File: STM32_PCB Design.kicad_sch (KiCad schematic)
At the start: 17 parts, among them J1 USB_B_Micro, SW1 SW_SPDT, U1 STM32F103C8T6, Y1 16MHz

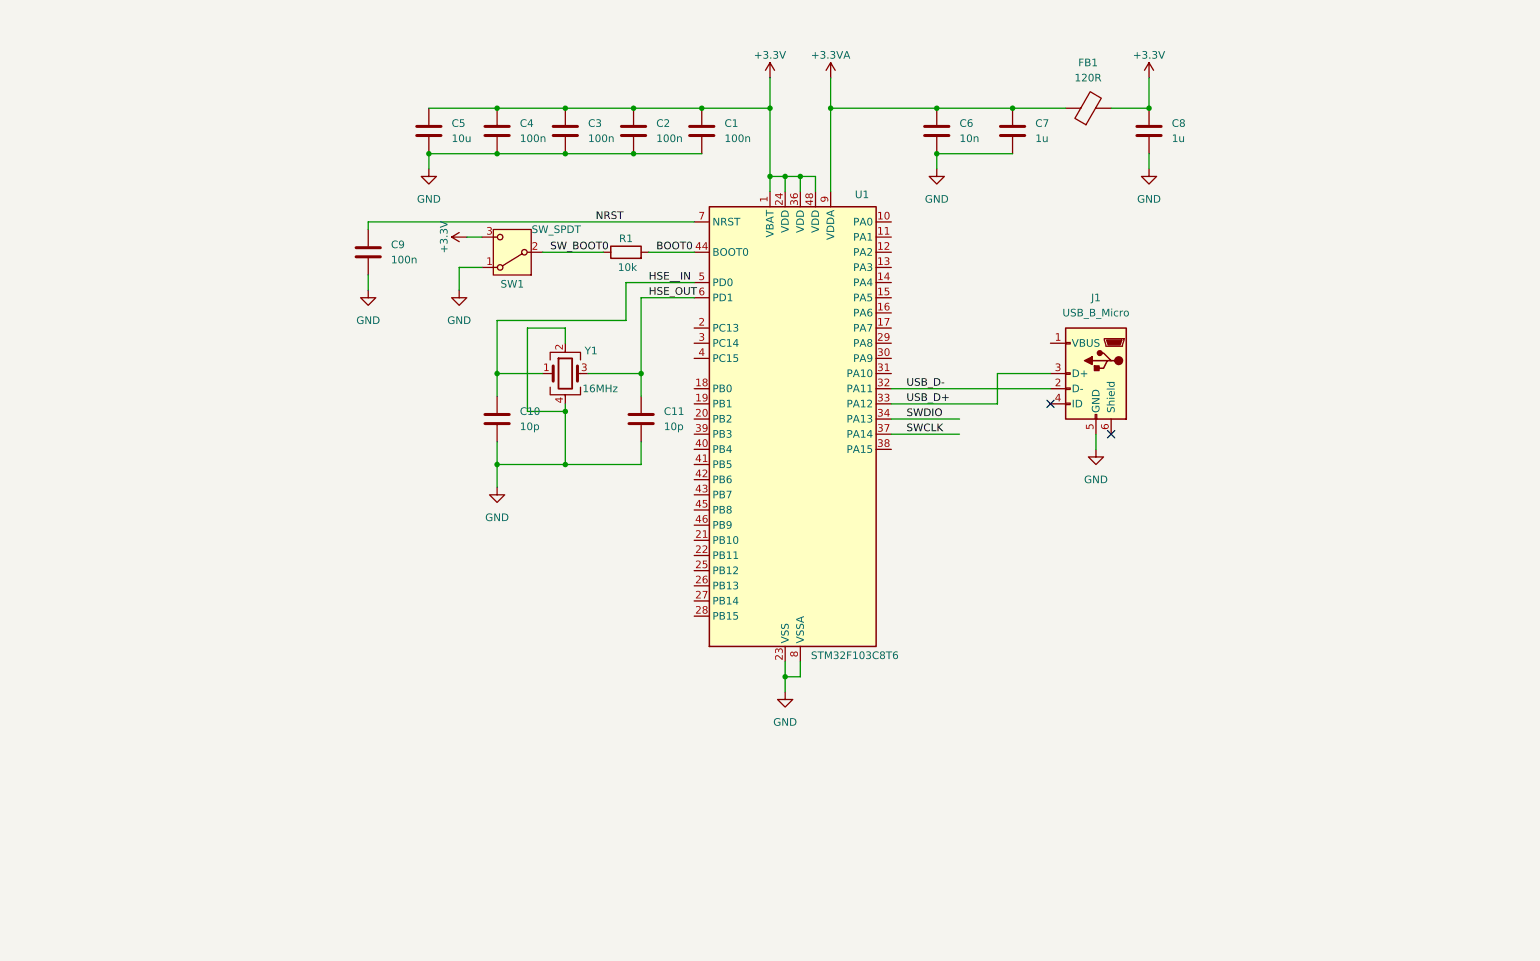
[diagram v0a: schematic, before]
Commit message: Added USART and I2C
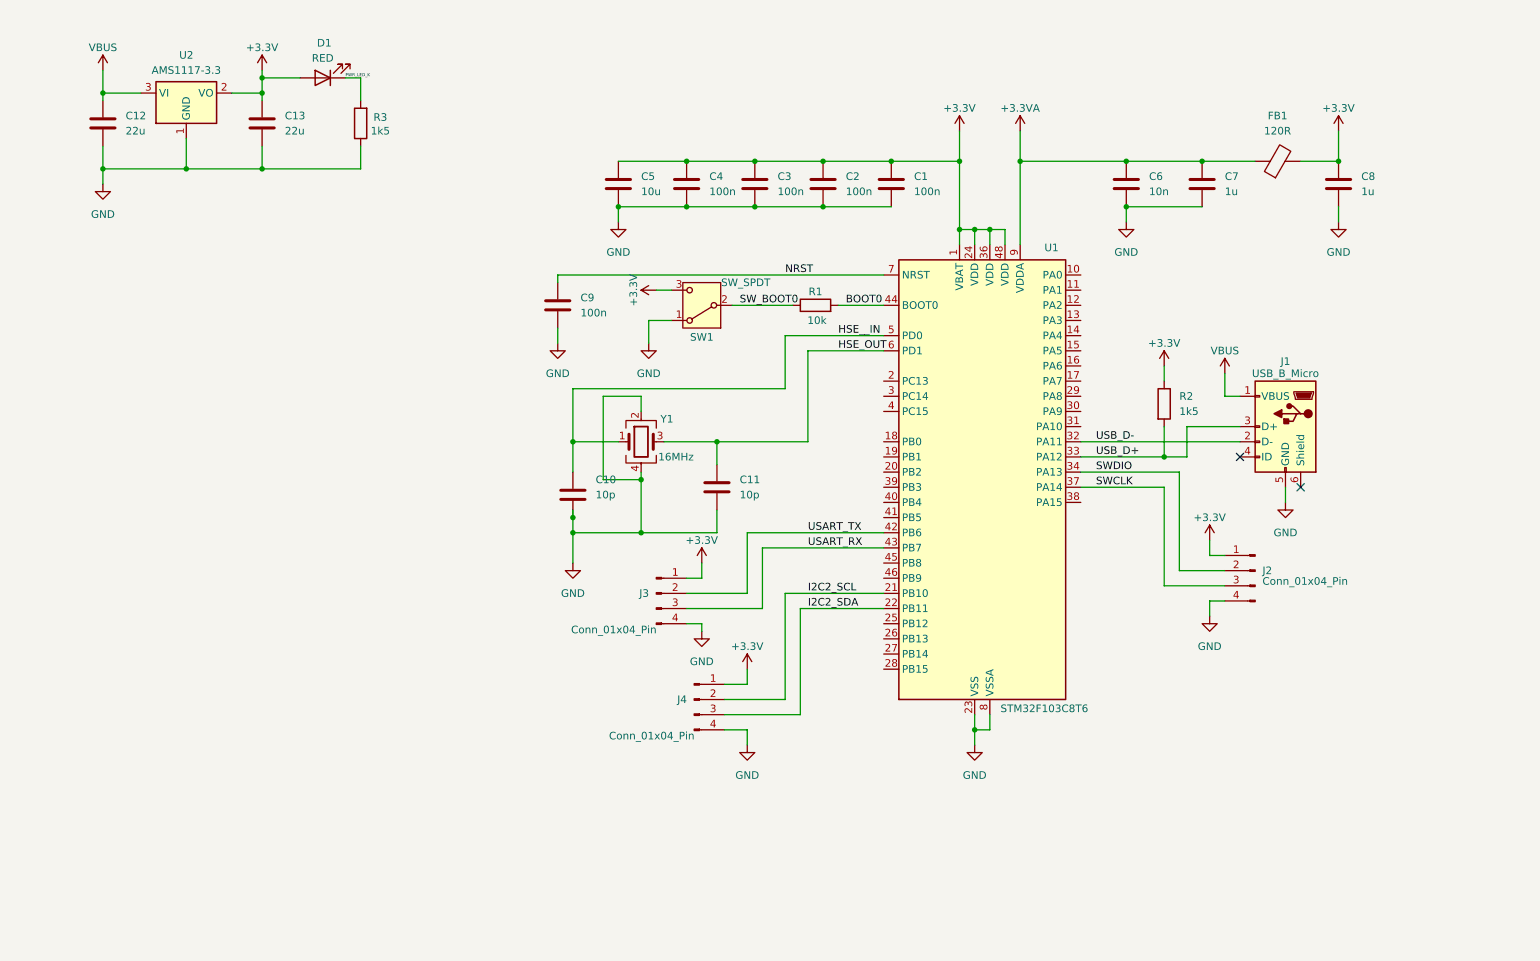
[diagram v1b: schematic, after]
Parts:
- added C12, C13: 22u, symbol Device:C
- added D1: RED, symbol Device:LED
- added J2, J3, J4: Conn_01x04_Pin, symbol Connector:Conn_01x04_Pin
- added R2, R3: 1k5, symbol Device:R
- added U2: AMS1117-3.3, Package_TO_SOT_SMD:SOT-223-3_TabPin2, symbol Regulator_Linear:AMS1117-3.3
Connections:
- net +3.3V: now also C13.1, D1.2 (A), J2.1 (Pin_1), J3.1 (Pin_1), J4.1 (Pin_1), R2.1, U2.2 (VO)
- net GND: now also C12.2, C13.2, J2.4 (Pin_4), J3.4 (Pin_4), J4.4 (Pin_4), R3.1, U2.1 (GND)
- net SWCLK: now also J2.3 (Pin_3)
- net SWDIO: now also J2.2 (Pin_2)
- net USB_D+: now also R2.2
- net I2C2_SCL: now reaches U1.21 (PB10)
- net I2C2_SCL: now also J4.2 (Pin_2)
- net I2C2_SDA: now reaches U1.22 (PB11)
- net I2C2_SDA: now also J4.3 (Pin_3)
- net USART_TX: now reaches U1.42 (PB6)
- net USART_TX: now also J3.2 (Pin_2)
- net USART_RX: now reaches U1.43 (PB7)
- net USART_RX: now also J3.3 (Pin_3)
- net VBUS: now reaches J1.1 (VBUS)
- net VBUS: now also C12.1, U2.3 (VI)
- new net PWR_LED_K: D1.1 (K), R3.2
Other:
- moved on the sheet: C1, C10, C11, C2, C3, C4, C5, C6, C7, C8, C9, FB1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

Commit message: Added mounting holes
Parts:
- added H1, H2, H3, H4: MountingHole, MountingHole:MountingHole_2.2mm_M2, symbol Mechanical:MountingHole
- added R4, R5: 1k5, Resistor_SMD:R_0402_1005Metric, symbol Device:R
- C1, C10, C11, C2, C3, C4, C6, C7, C8, C9: footprint (none) -> Capacitor_SMD:C_0402_1005Metric
- C12, C13: footprint (none) -> Capacitor_SMD:C_0805_2012Metric
- C5: footprint (none) -> Capacitor_SMD:C_0603_1608Metric
- D1: footprint (none) -> LED_SMD:LED_0603_1608Metric
- FB1: footprint (none) -> Inductor_SMD:L_0603_1608Metric
- J1: footprint (none) -> Connector_USB:USB_Micro-B_Wuerth_629105150521
- J2, J3, J4: footprint (none) -> Connector_PinHeader_2.54mm:PinHeader_1x04_P2.54mm_Vertical
- R1, R2, R3: footprint (none) -> Resistor_SMD:R_0402_1005Metric
- SW1: footprint (none) -> Button_Switch_SMD:SW_SPDT_PCM12
- Y1: footprint (none) -> Crystal:Crystal_SMD_3225-4Pin_3.2x2.5mm
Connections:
- net +3.3V: now also R4.1, R5.1
- net I2C2_SCL: now also R4.2
- net I2C2_SDA: now also R5.2
- no-connect marks 2 -> 29
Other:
- note added: "1x 100nF per VDD pin"
- note added: "CL = 2*(CL0-Cs)= 2/(10-5)pF"
- note added: "Microcontroller and USB circuit"
- note added: "Pin-out using STM32CubeMX"
- note added: "Power Supply"
- note added: "STM32 PCB Demo"
- note added: "USB App note AN4879"
- note added: "VBUS from USB connector (nom. +5V) Min. 22uF inp./outp. capacitors"
- note added: "VDDA Filtering"
- company: (none) -> _m.anasseh
- title: (none) -> STM32 PCB Demo
- moved on the sheet: C1, C10, C11, C12, C13, C2, C3, C4, C5, C6, C7, C8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
